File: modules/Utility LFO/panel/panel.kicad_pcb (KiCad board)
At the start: 2 copper layers, 80.9 x 133.4 mm, 18 parts

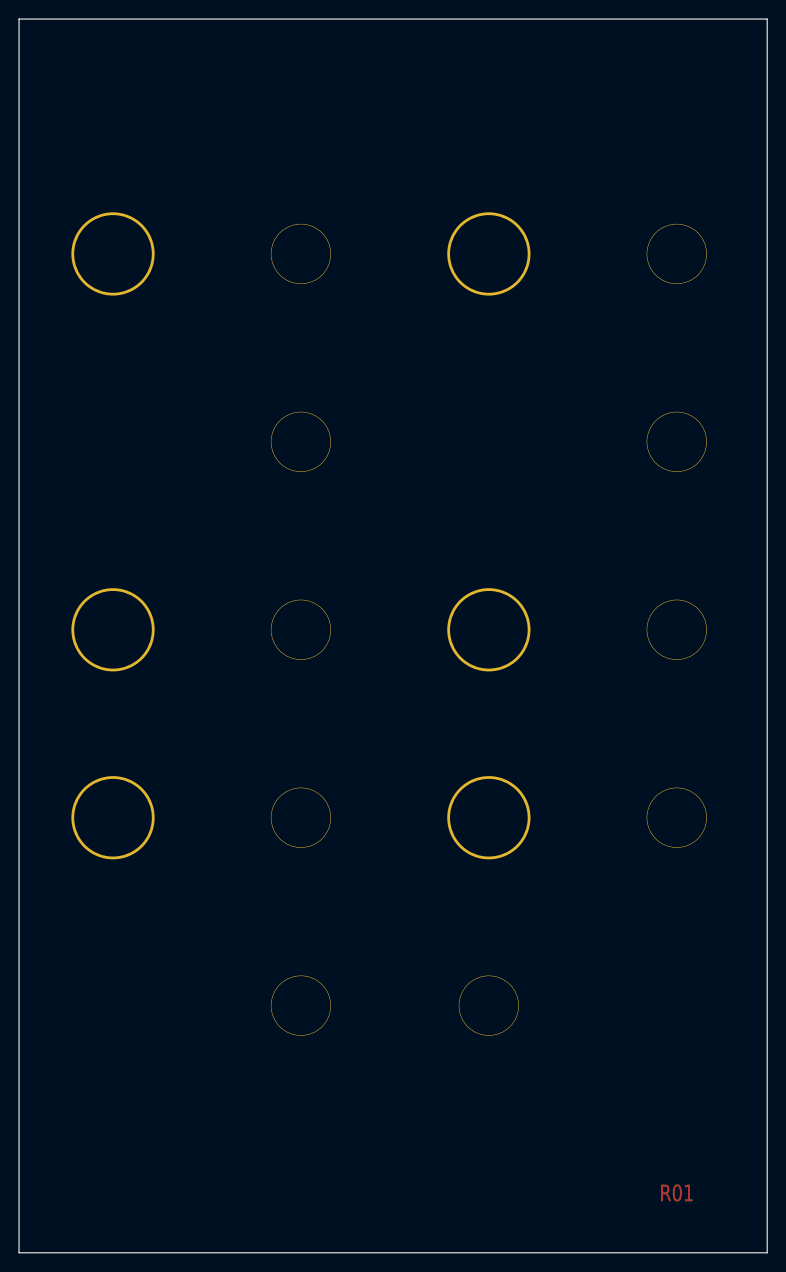
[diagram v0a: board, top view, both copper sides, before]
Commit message: update Utility LFO
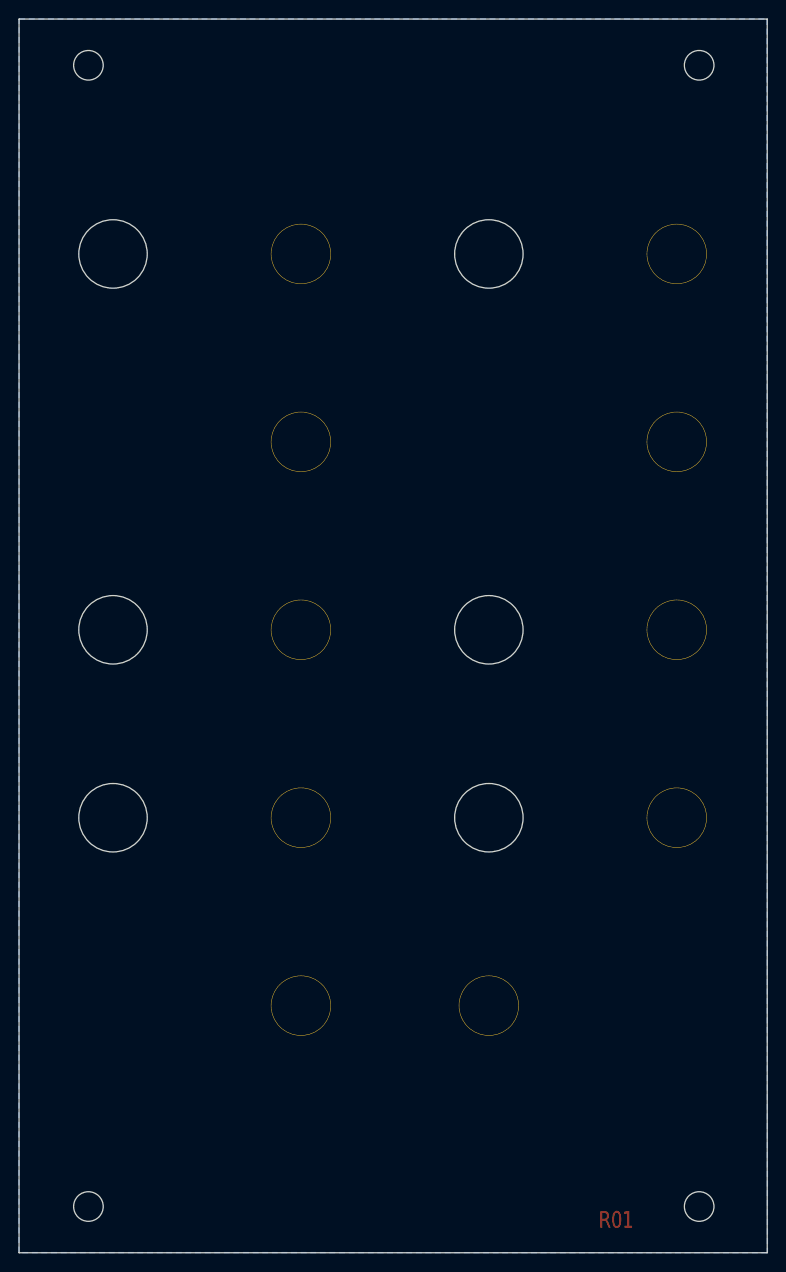
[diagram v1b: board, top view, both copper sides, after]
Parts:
- added REF**: MountingHole_3.2mm_M3, MountingHole:MountingHole_3.2mm_M3, F.Cu at (98.9, 153.8)
- added REF**: MountingHole_3.2mm_M3, MountingHole:MountingHole_3.2mm_M3, F.Cu at (32.9, 153.8)
- added REF**: MountingHole_3.2mm_M3, MountingHole:MountingHole_3.2mm_M3, F.Cu at (98.9, 30.4)
- added REF**: MountingHole_3.2mm_M3, MountingHole:MountingHole_3.2mm_M3, F.Cu at (32.9, 30.4)
- added pulse: G***, elektrophon:waveshape_pulse, F.Cu at (55.9, 71.1)
- added pulse: G***, elektrophon:waveshape_pulse, F.Cu at (96.5, 71.1)
- added svg2mod: G***, elektrophon:waveshape_triangle, F.Cu at (55.9, 91.4)
- added svg2mod: G***, elektrophon:waveshape_square, F.Cu at (55.9, 50.8)
- added svg2mod: G***, elektrophon:waveshape_triangle, F.Cu at (96.5, 91.4)
- added svg2mod: G***, elektrophon:waveshape_square, F.Cu at (96.5, 50.8)
- added vari: G***, elektrophon:waveshape_vari, F.Cu at (55.9, 111.8)
- added vari: G***, elektrophon:waveshape_vari, F.Cu at (96.5, 111.8)
- H1, H11, H12, H13, H2, H3: footprint elektrophon:panel_pot -> elektrophon:panel_potentiometer
- moved H14 62.8 mm to (96.5, 132.1)
- moved H4 61.2 mm to (35.6, 132.1)
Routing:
- added copper zone on B.Cu, net (none)
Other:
- board text added: "join"
- board text added: "shape"
- board text added: "speed"
- board text added: "swap"
- board text added: "vari"

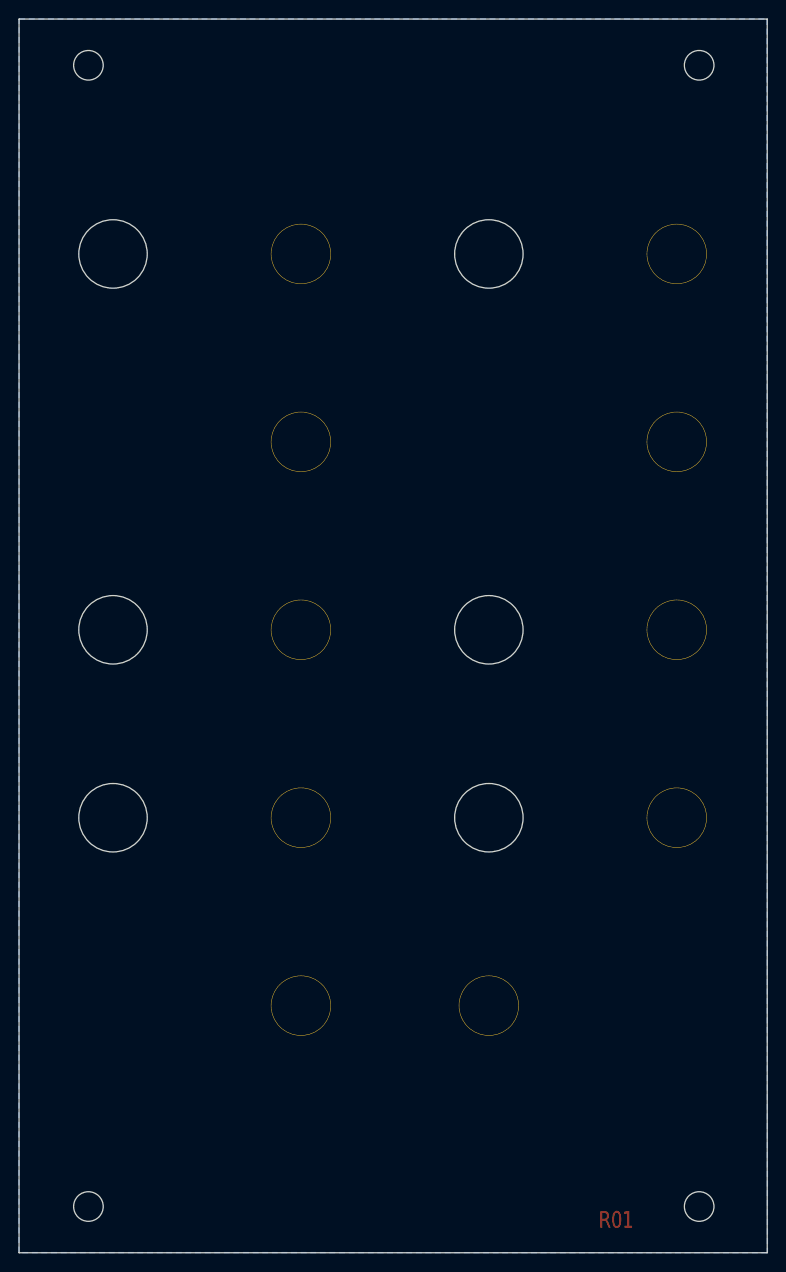
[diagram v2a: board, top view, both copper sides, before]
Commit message: add panel images
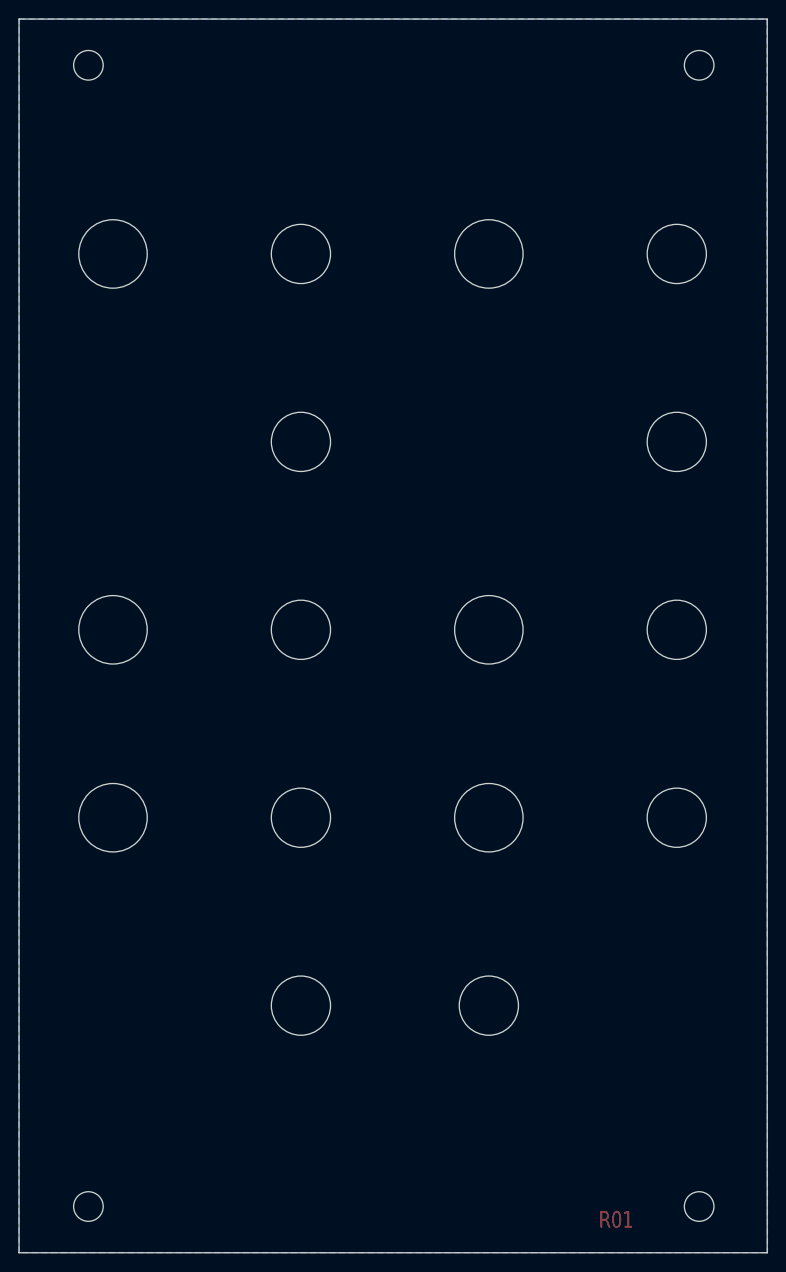
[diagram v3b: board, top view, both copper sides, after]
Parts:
- H10, H9: footprint elektrophon:SWITCH_HOLE -> elektrophon:panel_switch
- H15, H16, H17, H18, H5, H6, H7, H8: footprint elektrophon:JACK_HOLE -> elektrophon:panel_jack
